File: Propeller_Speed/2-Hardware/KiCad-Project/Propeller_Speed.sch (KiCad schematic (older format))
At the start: 4 parts, among them P1 CONN_1x3

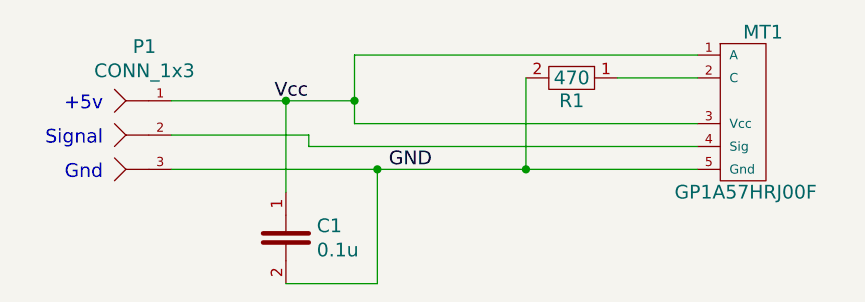
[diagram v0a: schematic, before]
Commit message: Modified resistor value
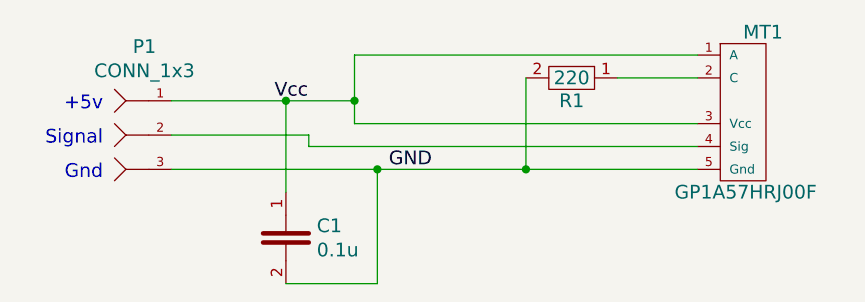
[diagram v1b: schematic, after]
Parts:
- R1: value 470 -> 220
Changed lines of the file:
@@
 P 8500 3300
 F 0 "R1" V 8600 3300 60  0000 C CNN
-F 1 "470" V 8500 3300 60  0000 C CNN
+F 1 "220" V 8500 3300 60  0000 C CNN
 F 2 "SMD:SMD_0805" V 8240 3200 60  0001 C CNN
 F 3 "" V 8340 3300 60  0001 C CNN
